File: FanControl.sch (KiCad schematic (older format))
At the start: 4 parts

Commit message: Add missing files from the TMC2130 branch.
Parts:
- R50, R51: footprint Resistor_SMD:R_0603_1608Metric -> PrntrBoardV1:R_0603_1608Metric
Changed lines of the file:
@@
 F 0 "R57" V 4293 3500 50  0000 C CNN
 F 1 "1k" V 4384 3500 50  0000 C CNN
-F 2 "Resistor_SMD:R_0603_1608Metric" V 4430 3500 50  0001 C CNN
+F 2 "PrntrBoardV1:R_0603_1608Metric" V 4430 3500 50  0001 C CNN
 F 3 "~" H 4500 3500 50  0001 C CNN
 	1    4500 3500
@@
 F 0 "R56" H 4320 3796 50  0000 L CNN
 F 1 "10k" H 4320 3705 50  0000 L CNN
-F 2 "Resistor_SMD:R_0603_1608Metric" V 4180 3750 50  0001 C CNN
+F 2 "PrntrBoardV1:R_0603_1608Metric" V 4180 3750 50  0001 C CNN
 F 3 "~" H 4250 3750 50  0001 C CNN
 	1    4250 3750

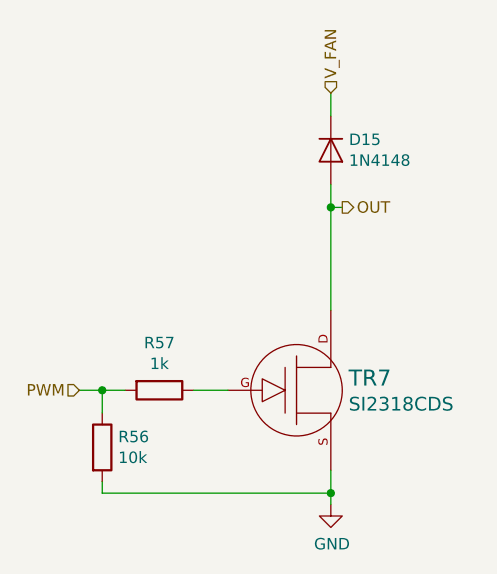
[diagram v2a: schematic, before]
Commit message: Reset schematics for tmc2660. Clean the board layout.
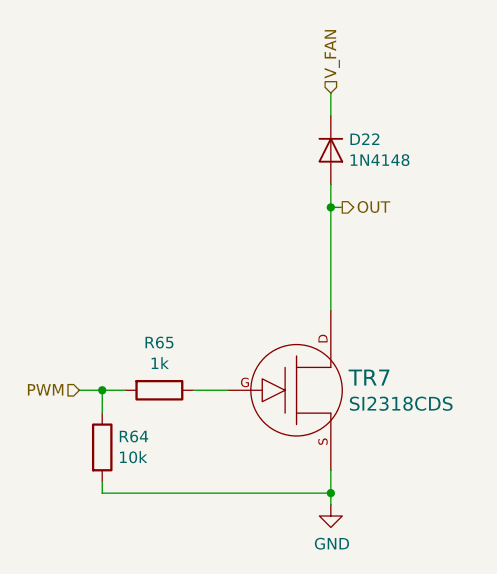
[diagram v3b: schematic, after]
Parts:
- renumbered D12 to D19, R50 to R58, R51 to R59
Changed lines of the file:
@@
 $EndDescr
 $Comp
-L Device:R R51
+L Device:R R59
 U 1 1 5AB90282
 P 4500 3500
-AR Path="/5AB9002A/5AB90282" Ref="R51"  Part="1"
-AR Path="/5AB91A5D/5AB90282" Ref="R53"  Part="1"
-AR Path="/5AB91A68/5AB90282" Ref="R55"  Part="1"
-AR Path="/5AB91A71/5AB90282" Ref="R57"  Part="1"
-F 0 "R57" V 4293 3500 50  0000 C CNN
+AR Path="/5AB9002A/5AB90282" Ref="R59"  Part="1"
+AR Path="/5AB91A5D/5AB90282" Ref="R61"  Part="1"
+AR Path="/5AB91A68/5AB90282" Ref="R63"  Part="1"
+AR Path="/5AB91A71/5AB90282" Ref="R65"  Part="1"
+F 0 "R65" V 4293 3500 50  0000 C CNN
 F 1 "1k" V 4384 3500 50  0000 C CNN
 F 2 "PrntrBoardV1:R_0603_1608Metric" V 4430 3500 50  0001 C CNN
@@
 $EndComp
 $Comp
-L power:GND #PWR071
+L power:GND #PWR082
 U 1 1 5AB906E9
 P 5250 4000
-AR Path="/5AB9002A/5AB906E9" Ref="#PWR071"  Part="1"
-AR Path="/5AB91A5D/5AB906E9" Ref="#PWR072"  Part="1"
-AR Path="/5AB91A68/5AB906E9" Ref="#PWR073"  Part="1"
-AR Path="/5AB91A71/5AB906E9" Ref="#PWR074"  Part="1"
-F 0 "#PWR074" H 5250 3750 50  0001 C CNN
+AR Path="/5AB9002A/5AB906E9" Ref="#PWR082"  Part="1"
+AR Path="/5AB91A5D/5AB906E9" Ref="#PWR083"  Part="1"
+AR Path="/5AB91A68/5AB906E9" Ref="#PWR084"  Part="1"
+AR Path="/5AB91A71/5AB906E9" Ref="#PWR085"  Part="1"
+F 0 "#PWR085" H 5250 3750 50  0001 C CNN
 F 1 "GND" H 5255 3827 50  0000 C CNN
 F 2 "" H 5250 4000 50  0001 C CNN
@@
 	5250 2700 5250 3150
 $Comp
-L Device:R R50
+L Device:R R58
 U 1 1 5AB969B0
 P 4250 3750
-AR Path="/5AB9002A/5AB969B0" Ref="R50"  Part="1"
-AR Path="/5AB91A5D/5AB969B0" Ref="R52"  Part="1"
-AR Path="/5AB91A68/5AB969B0" Ref="R54"  Part="1"
-AR Path="/5AB91A71/5AB969B0" Ref="R56"  Part="1"
-F 0 "R56" H 4320 3796 50  0000 L CNN
+AR Path="/5AB9002A/5AB969B0" Ref="R58"  Part="1"
+AR Path="/5AB91A5D/5AB969B0" Ref="R60"  Part="1"
+AR Path="/5AB91A68/5AB969B0" Ref="R62"  Part="1"
+AR Path="/5AB91A71/5AB969B0" Ref="R64"  Part="1"
+F 0 "R64" H 4320 3796 50  0000 L CNN
 F 1 "10k" H 4320 3705 50  0000 L CNN
 F 2 "PrntrBoardV1:R_0603_1608Metric" V 4180 3750 50  0001 C CNN
@@
 	5250 3950 5250 4000
 $Comp
-L Device:D D12
+L Device:D D19
 U 1 1 5AB96AD6
 P 5250 2450
-AR Path="/5AB9002A/5AB96AD6" Ref="D12"  Part="1"
-AR Path="/5AB91A5D/5AB96AD6" Ref="D13"  Part="1"
-AR Path="/5AB91A68/5AB96AD6" Ref="D14"  Part="1"
-AR Path="/5AB91A71/5AB96AD6" Ref="D15"  Part="1"
-F 0 "D15" V 5204 2529 50  0000 L CNN
+AR Path="/5AB9002A/5AB96AD6" Ref="D19"  Part="1"
+AR Path="/5AB91A5D/5AB96AD6" Ref="D20"  Part="1"
+AR Path="/5AB91A68/5AB96AD6" Ref="D21"  Part="1"
+AR Path="/5AB91A71/5AB96AD6" Ref="D22"  Part="1"
+F 0 "D22" V 5204 2529 50  0000 L CNN
 F 1 "1N4148" V 5295 2529 50  0000 L CNN
 F 2 "Diode_SMD:D_SOD-323_HandSoldering" H 5250 2450 50  0001 C CNN
